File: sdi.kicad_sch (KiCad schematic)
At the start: 46 parts, among them J2 031-70526-21, J3 031-70526-21, U10 GS2971A, U9 GS2988, Y1 ABM7_27.000MH_D2Y_T

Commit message: Added loclib
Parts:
- C43, C44: footprint antmicro-footprints:0603-cap -> crosslink-nx-video-converter-footprints:0603-cap; symbol antmicroCapacitors0603:C_33p_0603 -> crosslink-nx-video-converter:C_33p_0603
- C45, C46, C49: footprint antmicro-footprints:0402-cap -> crosslink-nx-video-converter-footprints:0402-cap; symbol antmicroCapacitors0402:C_1u_0402 -> crosslink-nx-video-converter:C_1u_0402
- C47: footprint antmicro-footprints:0603-cap -> crosslink-nx-video-converter-footprints:0603-cap; symbol antmicroCapacitors0603:C_47n_0603 -> crosslink-nx-video-converter:C_47n_0603
- C48, C50: footprint antmicro-footprints:0603-cap -> crosslink-nx-video-converter-footprints:0603-cap; symbol antmicroCapacitors0603:C_470n_0603 -> crosslink-nx-video-converter:C_470n_0603
- C51: footprint antmicro-footprints:0402-cap -> crosslink-nx-video-converter-footprints:0402-cap; symbol antmicroCapacitors0402:C_10n_0402 -> crosslink-nx-video-converter:C_10n_0402
- C52, C53: footprint antmicro-footprints:0402-cap -> crosslink-nx-video-converter-footprints:0402-cap; symbol antmicroCapacitors0402:C_4u7_0402 -> crosslink-nx-video-converter:C_4u7_0402
- C54, C55, C56, C57, C58, C59, C60, C61, C62, C64, C65, C66, C67: footprint antmicro-footprints:0603-cap -> crosslink-nx-video-converter-footprints:0603-cap; symbol antmicroCapacitors0603:C_100n_0603 -> crosslink-nx-video-converter:C_100n_0603
- C63: footprint antmicro-footprints:0603-cap -> crosslink-nx-video-converter-footprints:0603-cap; symbol antmicroCapacitorspol:C_33u_0603 -> crosslink-nx-video-converter:C_33u_0603
- J2, J3: footprint antmicro-footprints:BNC_Edge_Conn -> crosslink-nx-video-converter-footprints:BNC_Edge_Conn; symbol antmicroCoaxialConnectorsRF:031-70526-21 -> crosslink-nx-video-converter:031-70526-21
- L4, L5: footprint antmicro-footprints:0402-cap -> crosslink-nx-video-converter-footprints:0402-cap; symbol antmicroFixedInductors:L_0402_6n2 -> crosslink-nx-video-converter:L_0402_6n2
- R55, R56, R62, R63, R64, R65: footprint antmicro-footprints:0402-res -> crosslink-nx-video-converter-footprints:0402-res; symbol antmicroResistors0402:R_75R_0402 -> crosslink-nx-video-converter:R_75R_0402
- R57: footprint antmicro-footprints:0402-res -> crosslink-nx-video-converter-footprints:0402-res; symbol antmicroResistors0402:R_37R4_0402 -> crosslink-nx-video-converter:R_37R4_0402
- R58: footprint antmicro-footprints:0603-res -> crosslink-nx-video-converter-footprints:0603-res; symbol antmicroResistors0603:R_750R_0603 -> crosslink-nx-video-converter:R_750R_0603
- R59: footprint antmicro-footprints:0603-res -> crosslink-nx-video-converter-footprints:0603-res; symbol antmicroResistors0603:R_0R_0603 -> crosslink-nx-video-converter:R_0R_0603
- R60, R61: footprint antmicro-footprints:0603-res -> crosslink-nx-video-converter-footprints:0603-res; symbol antmicroResistors0603:R_100k_0603 -> crosslink-nx-video-converter:R_100k_0603
- R66: footprint antmicro-footprints:0402-res -> crosslink-nx-video-converter-footprints:0402-res; symbol antmicroResistors0402:R_105R_0402 -> crosslink-nx-video-converter:R_105R_0402
- TP14, TP15: footprint antmicro-footprints:TP-R-1.5 -> crosslink-nx-video-converter-footprints:TP-R-1.5; symbol antmicroTestPoints:TP -> crosslink-nx-video-converter:TP
- U10: footprint antmicro-footprints:BGA100_11x11mm -> crosslink-nx-video-converter-footprints:BGA100_11x11mm; symbol antmicroInterfaceControllers:GS2971A -> crosslink-nx-video-converter:GS2971A
- U9: footprint antmicro-footprints:QFN-16_EP_4x4_Pitch0.65mm -> crosslink-nx-video-converter-footprints:QFN-16_EP_4x4_Pitch0.65mm; symbol antmicroInterfaceControllers:GS2988 -> crosslink-nx-video-converter:GS2988
- Y1: footprint antmicro-footprints:ABM7_OSC -> crosslink-nx-video-converter-footprints:ABM7_OSC; symbol antmicroOscillators:ABM7_27.000MH_D2Y_T -> crosslink-nx-video-converter:ABM7_27.000MH_D2Y_T

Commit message: Divided FPGA into multiple blocks
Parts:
- added C? (x3): C_100n_0603, crosslink-nx-video-converter-footprints:0603-cap, symbol crosslink-nx-video-converter:C_100n_0603
- added U? (x3): LIFCL-40-9BG256C, antmicro-footprints:BGA-256_16x16_14.0x14.0mm, symbol antmicroBGAchips:LIFCL-40-9BG256C
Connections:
- net +3V3: now also C?.1, C?.1, C?.1, U?.F5 (VCCIO7), U?.J13 (VCCIO2), U?.J4 (VCCIO6)
- net 20bit/~{10bit}: now also U?.J15 (PR34B)
- net AUDIO_EN/~{DIS}: now also U?.J11 (PR36A)
- net DVB_ASI: now also U?.H12 (PR32B)
- net GND: now also C?.2, C?.2, C?.2
- net IOPROC_EN/~{DIS}: now also U?.J12 (PR36B)
- net JTAG/~{HOST}: now also U?.K11 (PR38A)
- net RESET_TRST: now also U?.D4 (PL3A/ULC_GPLL0T_IN)
- net SCLK_TCK: now also U?.E5 (PL6B)
- net SDIN_TDI: now also U?.F6 (PL17A/PCLKT7_2)
- net SDI_D0: now also U?.H6 (PL24A)
- net SDI_D1: now also U?.H5 (PL24B)
- net SDI_D10: now also U?.K2 (PL34B)
- net SDI_D11: now also U?.K4 (PL36A)
- net SDI_D12: now also U?.K3 (PL36B)
- net SDI_D13: now also U?.K6 (PL38A)
- net SDI_D14: now also U?.K5 (PL38B)
- net SDI_D15: now also U?.L1 (PL40A)
- net SDI_D16: now also U?.L2 (PL40B)
- net SDI_D17: now also U?.M1 (PL42A)
- net SDI_D18: now also U?.M2 (PL42B)
- net SDI_D19: now also U?.L4 (PL46A)
- net SDI_D2: now also U?.H4 (PL26A)
- net SDI_D3: now also U?.H3 (PL26B)
- net SDI_D4: now also U?.H1 (PL27A)
- net SDI_D5: now also U?.H2 (PL27B)
- net SDI_D6: now also U?.J5 (PL30B)
- net SDI_D7: now also U?.J1 (PL32A/PCLKT6_1)
- net SDI_D8: now also U?.J2 (PL32B)
- net SDI_D9: now also U?.K1 (PL34A/PCLKT6_2)
- net SDI_PCLK: now also U?.J6 (PL30A/PCLKT6_0)
- net SDI_STAT0: now also U?.L5 (PL46B)
- net SDI_STAT1: now also U?.M3 (PL47A)
- net SDI_STAT2: now also U?.L3 (PL47B)
- net SDI_STAT3: now also U?.N2 (PL49A)
- net SDI_STAT4: now also U?.N1 (PL49B)
- net SDI_STAT5: now also U?.G3 (PL20A/PCLKT7_0)
- net SDOUT_TDO: now also U?.F4 (PL19A/PCLKT7_1)
- net SDO_EN/DIS: now also U?.G6 (PL17B)
- net STANDBY: now also U?.D5 (PL3B/ULC_GPLL0C_IN)
- net SW_EN: now also U?.D6 (PL4A)
- net TIM_861: now also U?.E6 (PL4B)
- net ~{CS_TMS}: now also U?.E4 (PL6A)
- net ~{RC_BYP}: now also U?.K12 (PR38B)
- net ~{SDO_DISABLE}: now also U?.G4 (PL19B)
- net ~{SMPTE_BYPASS}: now also U?.J16 (PR34A/PCLKT2_2)
- new net DIP0: U?.H16 (PR26A)
- new net DIP1: U?.H15 (PR27A)
- new net DIP2: U?.H14 (PR27B)
- new net DIP3: U?.H11 (PR30A/PCLKT2_0)
- new net DIP4: U?.H10 (PR30B)
- new net DIP5: U?.H13 (PR32A/PCLKT2_1)
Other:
- note added: "FPGA"
- moved on the sheet: C43, C44, C45, C46, C47, C48, C49, C50, C51, C52, C53, C54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

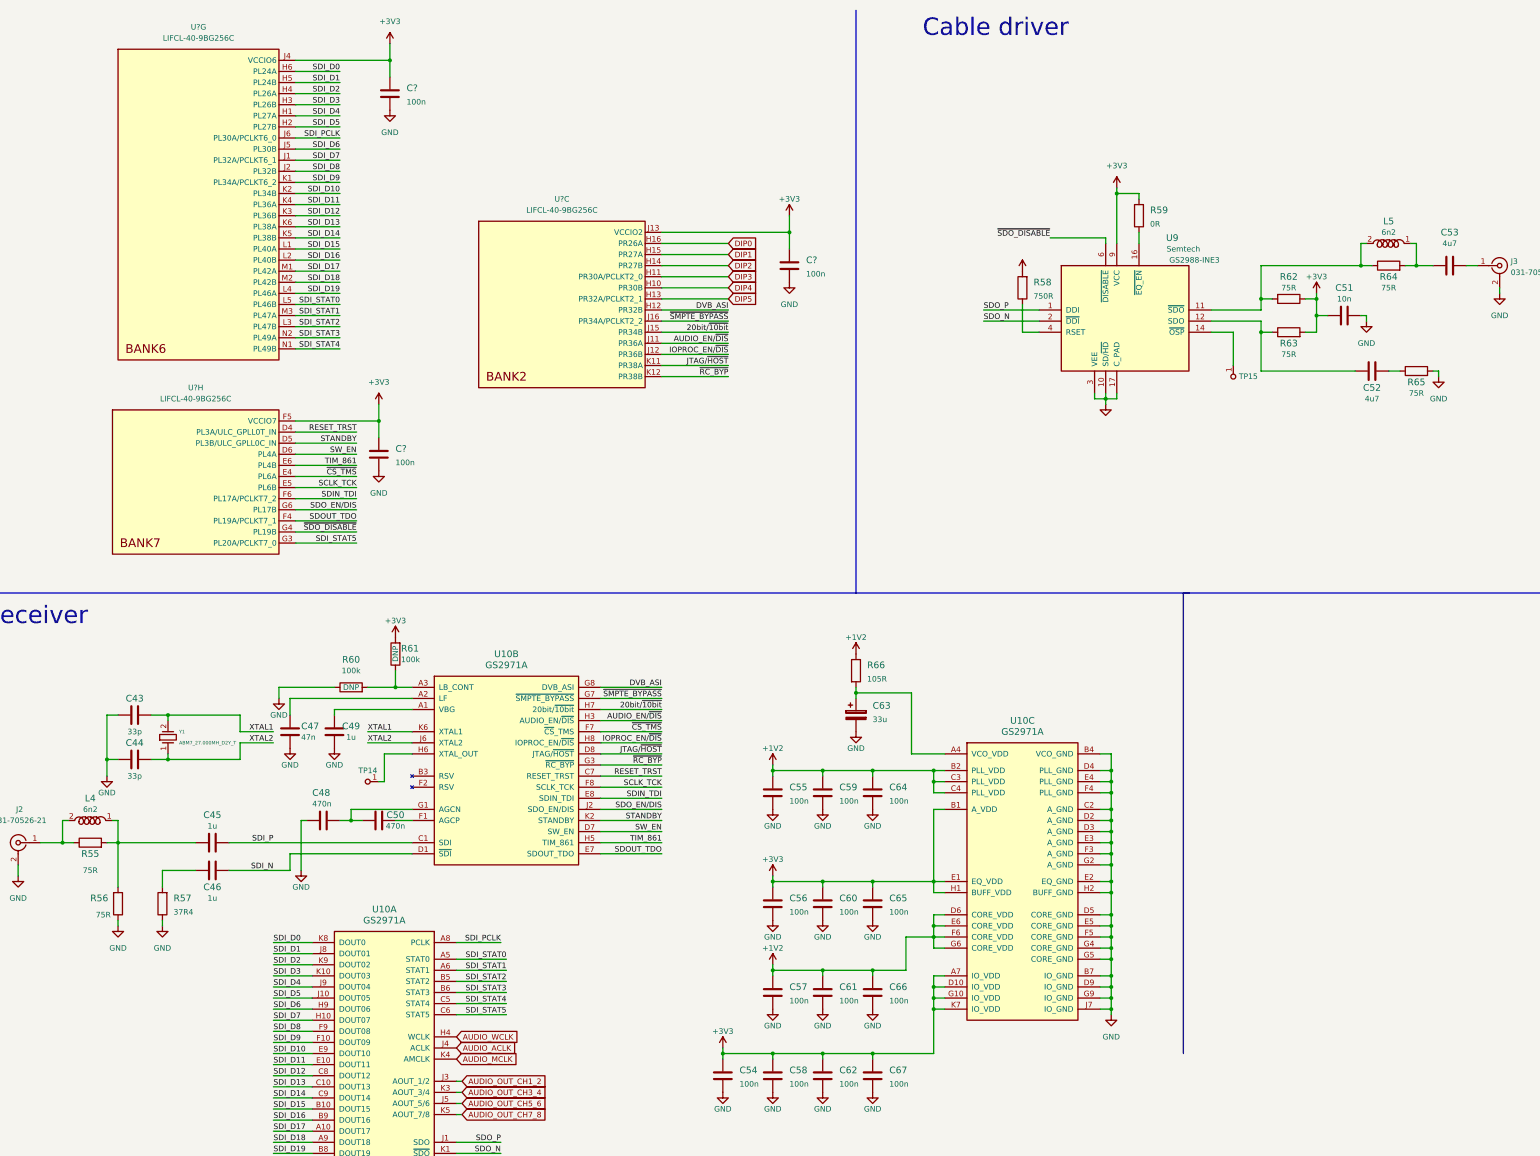
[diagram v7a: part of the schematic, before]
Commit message: Modified power indicator and connected unused pins
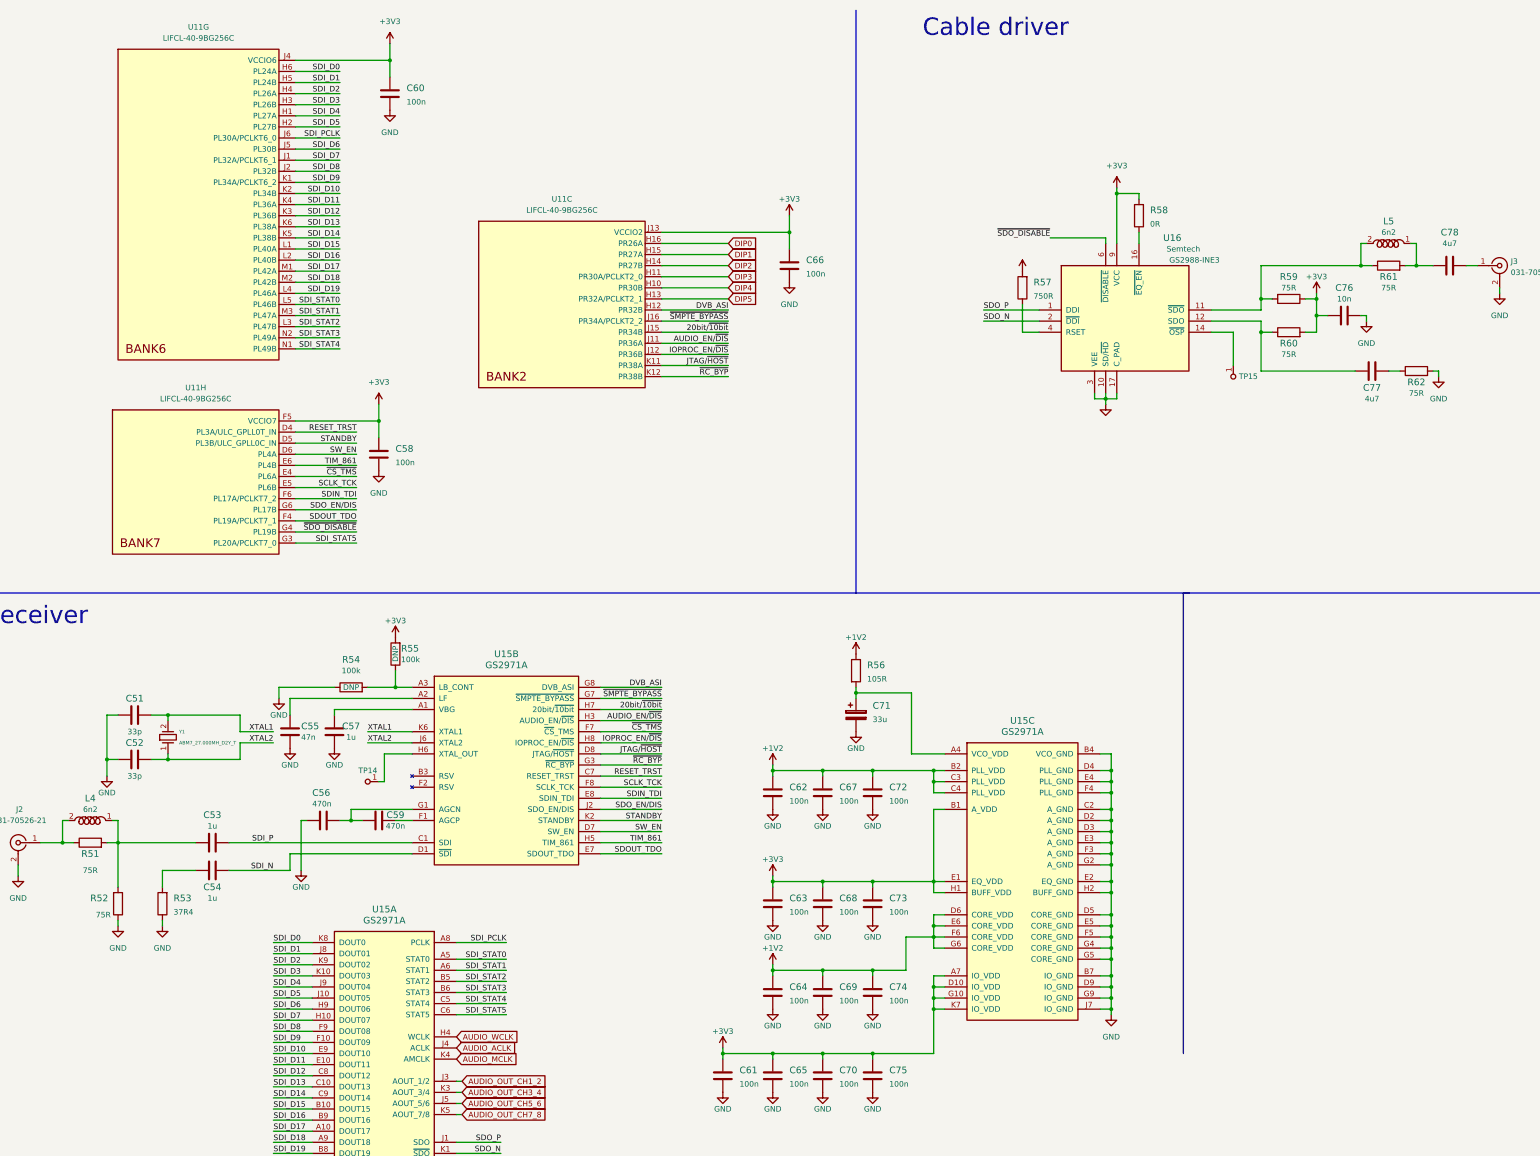
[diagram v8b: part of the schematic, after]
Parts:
- gave numbers to parts that had none: 4
- renumbered C43 to C51, C44 to C52, C45 to C53, C46 to C54, C47 to C55, C48 to C56, C49 to C57, C50 to C59, C54 to C61, C55 to C62, C56 to C63, C57 to C64, C58 to C65, C59 to C67, C60 to C68, C61 to C69, C62 to C70, C63 to C71, C64 to C72, C65 to C73, C66 to C74, C67 to C75, C51 to C76, C52 to C77, C53 to C78, R55 to R51, R56 to R52, R57 to R53, R60 to R54, R61 to R55, R66 to R56, R58 to R57, R59 to R58, R62 to R59, R63 to R60, R64 to R61, R65 to R62, U10 to U15, U9 to U16
